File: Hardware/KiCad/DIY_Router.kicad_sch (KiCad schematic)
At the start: 21 parts, among them IC1 HLK-7628N, IC2 TPS62A06ADRLR, J1 217179-0001, SW1 SW_Push

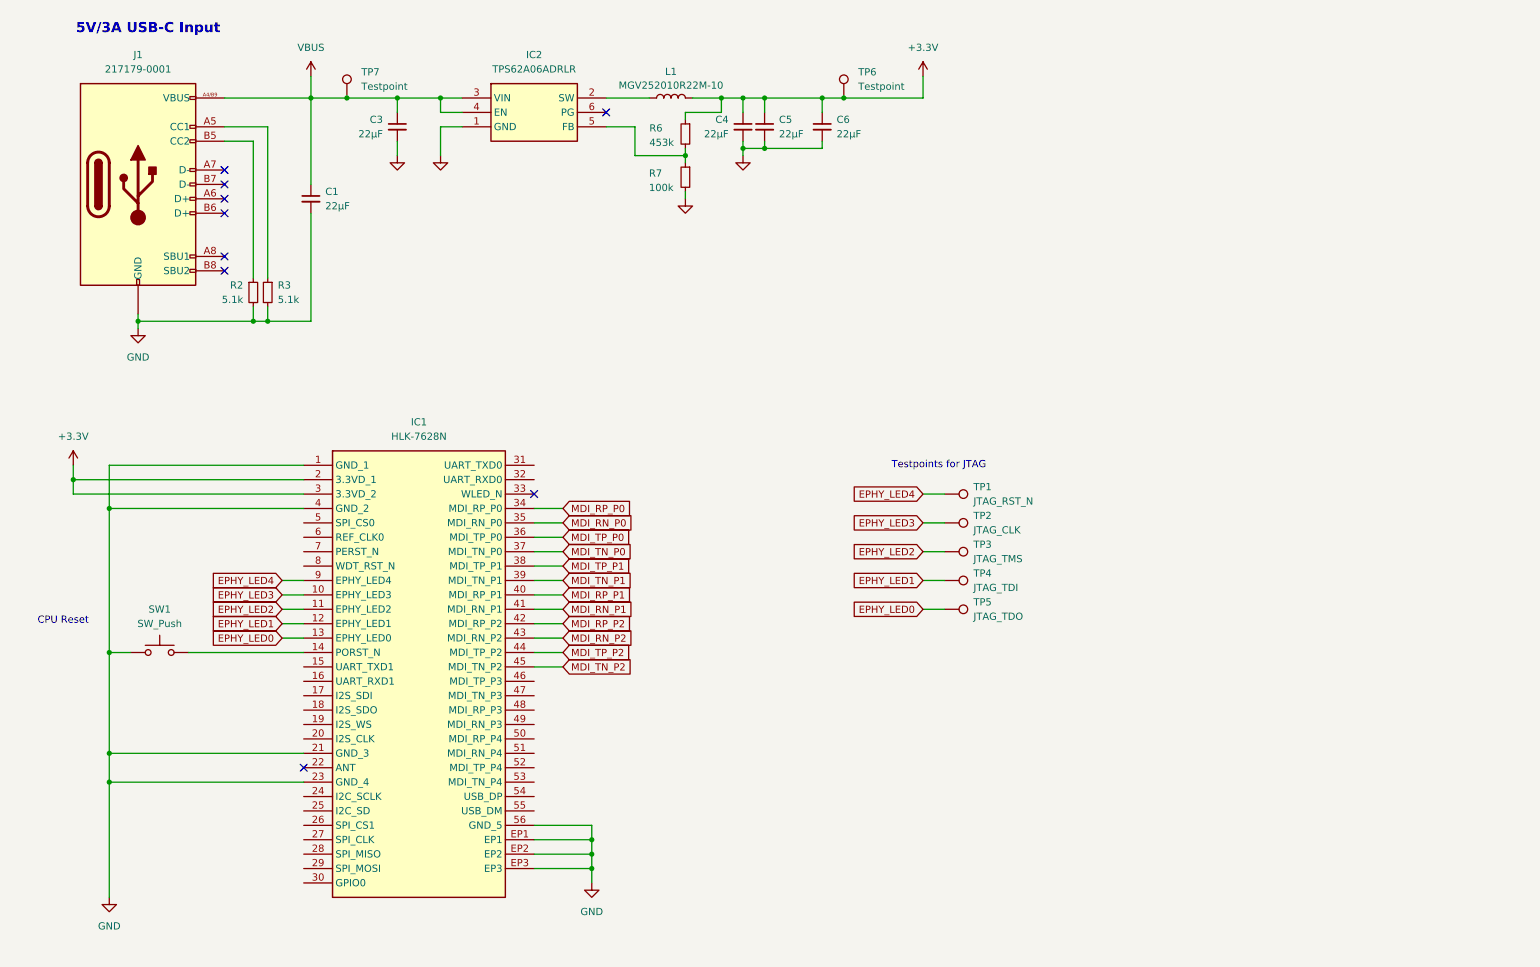
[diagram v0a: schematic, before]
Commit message: Add datasheet for MT7628 SOC Add footprints and symbol for Max Linear XR22801 USB Ethernet UART bridge Add sheet for XR22801 Add GPIO and JTAG headers in main sheet
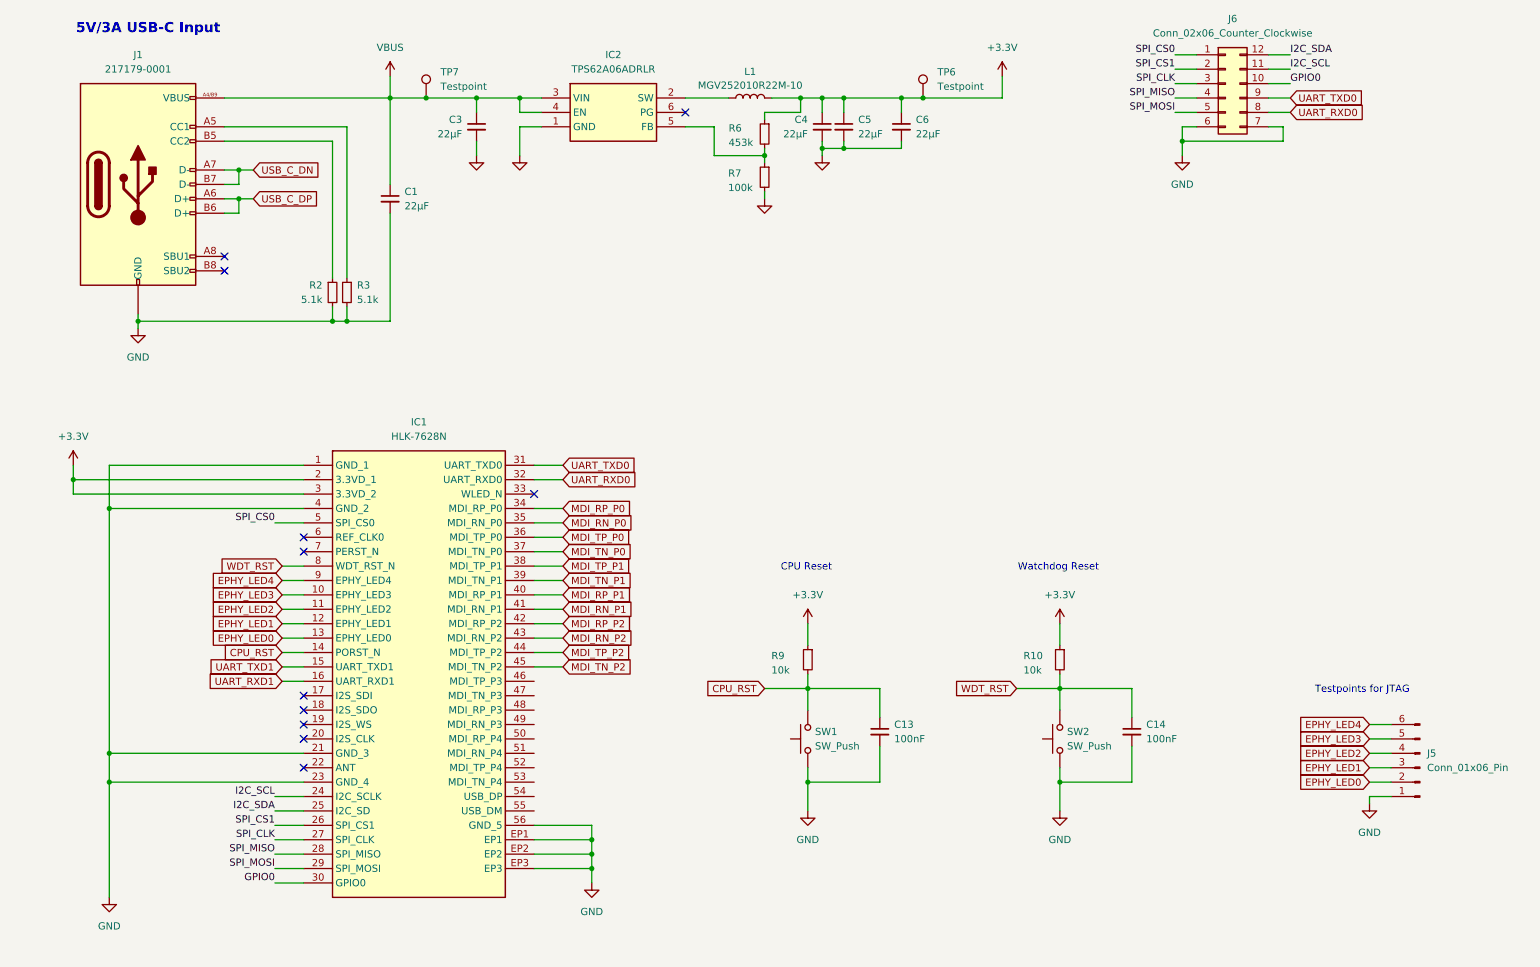
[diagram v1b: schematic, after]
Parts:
- removed TP1: JTAG_RST_N, symbol Connector:TestPoint
- removed TP2: JTAG_CLK, symbol Connector:TestPoint
- removed TP3: JTAG_TMS, symbol Connector:TestPoint
- removed TP4: JTAG_TDI, symbol Connector:TestPoint
- removed TP5: JTAG_TDO, symbol Connector:TestPoint
- added C13, C14: 100nF, Capacitor_SMD:C_0603_1608Metric, symbol Device:C_Small
- added J5: Conn_01x06_Pin, Connector_PinHeader_2.54mm:PinHeader_1x06_P2.54mm_Vertical, symbol Connector:Conn_01x06_Pin
- added J6: Conn_02x06_Counter_Clockwise, Connector_PinHeader_2.54mm:PinHeader_2x06_P2.54mm_Vertical, symbol Connector_Generic:Conn_02x06_Counter_Clockwise
- added R10, R9: 10k, Resistor_SMD:R_0402_1005Metric, symbol Device:R_Small
- added SW2: SW_Push, Button_Switch_SMD:SW_Push_1P1T-MP_NO_Horizontal_Alps_SKRTLAE010, symbol Switch:SW_Push
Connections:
- net +3.3V: now also R10.1, R9.1
- net EPHY_LED0: now also J5.2 (Pin_2)
- net EPHY_LED1: now also J5.3 (Pin_3)
- net EPHY_LED2: now also J5.4 (Pin_4)
- net EPHY_LED3: now also J5.5 (Pin_5)
- net EPHY_LED4: now also J5.6 (Pin_6)
- net GND: now also C13.2, C14.2, J5.1 (Pin_1), J6.6 (Pin_6), J6.7 (Pin_7), SW2.1
- net USB_C_DP: now reaches J1.A6 (D+)
- net USB_C_DP: now also J1.B6 (D+)
- net USB_C_DN: now reaches J1.A7 (D-)
- net USB_C_DN: now also J1.B7 (D-)
- net CPU_RST: now reaches IC1.14 (PORST_N), SW1.2
- net CPU_RST: now also C13.1, R9.2
- net UART_TXD1: now reaches IC1.15 (UART_TXD1)
- net UART_RXD1: now reaches IC1.16 (UART_RXD1)
- net I2C_SCL: now reaches IC1.24 (I2C_SCLK)
- net I2C_SCL: now also J6.11 (Pin_11)
- net I2C_SDA: now reaches IC1.25 (I2C_SD)
- net I2C_SDA: now also J6.12 (Pin_12)
- net SPI_CS1: now reaches IC1.26 (SPI_CS1)
- net SPI_CS1: now also J6.2 (Pin_2)
- net SPI_CLK: now reaches IC1.27 (SPI_CLK)
- net SPI_CLK: now also J6.3 (Pin_3)
- net SPI_MISO: now reaches IC1.28 (SPI_MISO)
- net SPI_MISO: now also J6.4 (Pin_4)
- net SPI_MOSI: now reaches IC1.29 (SPI_MOSI)
- net SPI_MOSI: now also J6.5 (Pin_5)
- net GPIO0: now reaches IC1.30 (GPIO0)
- net GPIO0: now also J6.10 (Pin_10)
- net UART_TXD0: now reaches IC1.31 (UART_TXD0)
- net UART_TXD0: now also J6.9 (Pin_9)
- net UART_RXD0: now reaches IC1.32 (UART_RXD0)
- net UART_RXD0: now also J6.8 (Pin_8)
- net SPI_CS0: now reaches IC1.5 (SPI_CS0)
- net SPI_CS0: now also J6.1 (Pin_1)
- net WDT_RST: now reaches IC1.8 (WDT_RST_N)
- net WDT_RST: now also C14.1, R10.2, SW2.2
- no-connect marks 9 -> 11
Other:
- note added: "Watchdog Reset"
- moved on the sheet: C1, C3, C4, C5, C6, IC2, L1, R2, R3, R6, R7, SW1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

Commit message: Add USB ESD protection USBLC6-2SC6Y Edit GPIO pin header
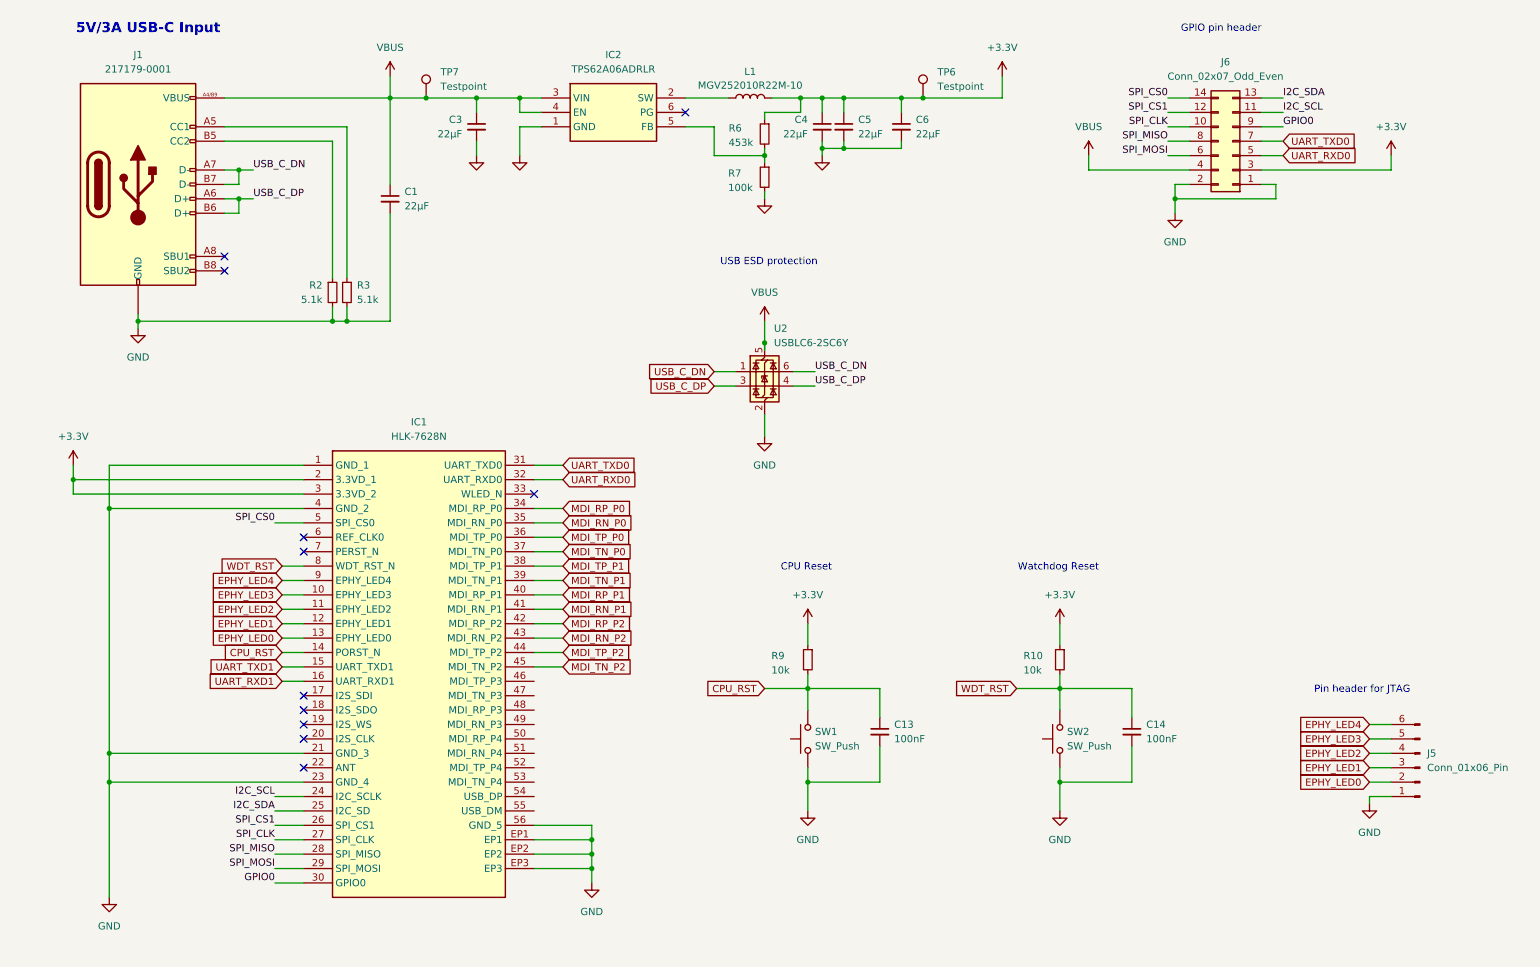
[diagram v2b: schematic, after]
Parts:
- removed J6: Conn_02x06_Counter_Clockwise, Connector_PinHeader_2.54mm:PinHeader_2x06_P2.54mm_Vertical, symbol Connector_Generic:Conn_02x06_Counter_Clockwise
- added J6: Conn_02x07_Odd_Even, Connector_PinHeader_2.54mm:PinHeader_2x07_P2.54mm_Vertical, symbol Connector_Generic:Conn_02x07_Odd_Even
- added U2: USBLC6-2SC6Y, Button_Switch_SMD:SW_DIP_SPSTx03_Slide_6.7x9.18mm_W6.73mm_P2.54mm_LowProfile_JPin, symbol Power_Protection:USBLC6-2SC6
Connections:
- net +3.3V: now also J6.3 (Pin_3)
- net GND: now also J6.1 (Pin_1), J6.2 (Pin_2), U2.2 (GND)
- net GPIO0: now also J6.9 (Pin_9)
- net I2C_SCL: now also J6.11 (Pin_11)
- net I2C_SDA: now also J6.13 (Pin_13)
- net SPI_CLK: now also J6.10 (Pin_10)
- net SPI_CS0: now also J6.14 (Pin_14)
- net SPI_CS1: now also J6.12 (Pin_12)
- net SPI_MISO: now also J6.8 (Pin_8)
- net SPI_MOSI: now also J6.6 (Pin_6)
- net UART_RXD0: now also J6.5 (Pin_5)
- net UART_TXD0: now also J6.7 (Pin_7)
- net USB_C_DN: now also U2.1 (I/O1), U2.6 (I/O1)
- net USB_C_DP: now also U2.3 (I/O2), U2.4 (I/O2)
- net VBUS: now also J6.4 (Pin_4), U2.5 (VBUS)
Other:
- note added: "GPIO pin header"
- note added: "Pin header for JTAG"
- note added: "USB ESD protection"
- note removed: "Testpoints for JTAG"

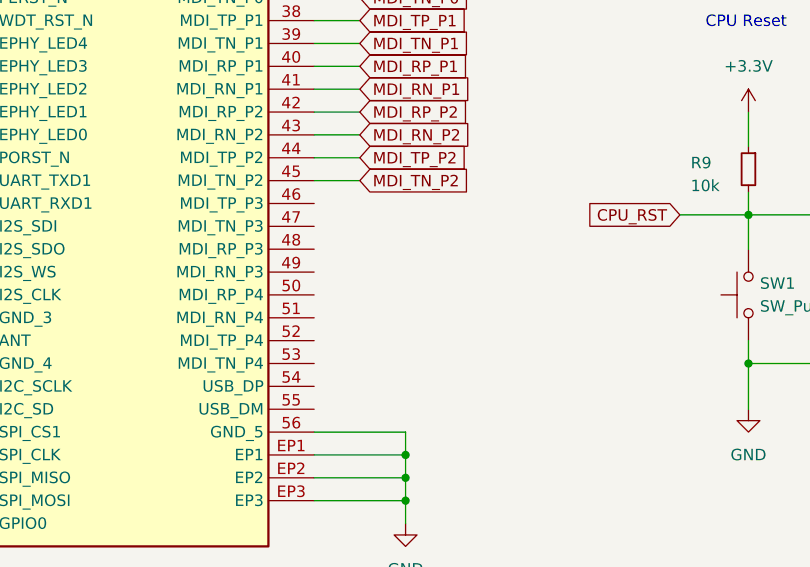
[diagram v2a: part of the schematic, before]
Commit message: USB_Bridge: add transformerless connection between usb bridge and SOM
- Ethernet: Add fourth rj45 jack
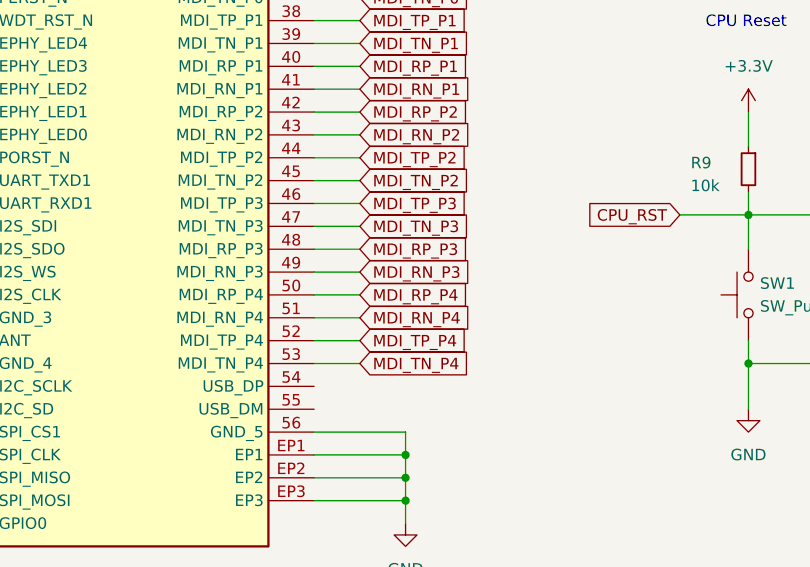
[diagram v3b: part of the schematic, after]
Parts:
- U2: footprint Button_Switch_SMD:SW_DIP_SPSTx03_Slide_6.7x9.18mm_W6.73mm_P2.54mm_LowProfile_JPin -> Package_TO_SOT_SMD:SOT-23-6
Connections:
- net MDI_TP_P3: now reaches IC1.46 (MDI_TP_P3)
- net MDI_TN_P3: now reaches IC1.47 (MDI_TN_P3)
- net MDI_RP_P3: now reaches IC1.48 (MDI_RP_P3)
- net MDI_RN_P3: now reaches IC1.49 (MDI_RN_P3)
- net MDI_RP_P4: now reaches IC1.50 (MDI_RP_P4)
- net MDI_RN_P4: now reaches IC1.51 (MDI_RN_P4)
- net MDI_TP_P4: now reaches IC1.52 (MDI_TP_P4)
- net MDI_TN_P4: now reaches IC1.53 (MDI_TN_P4)

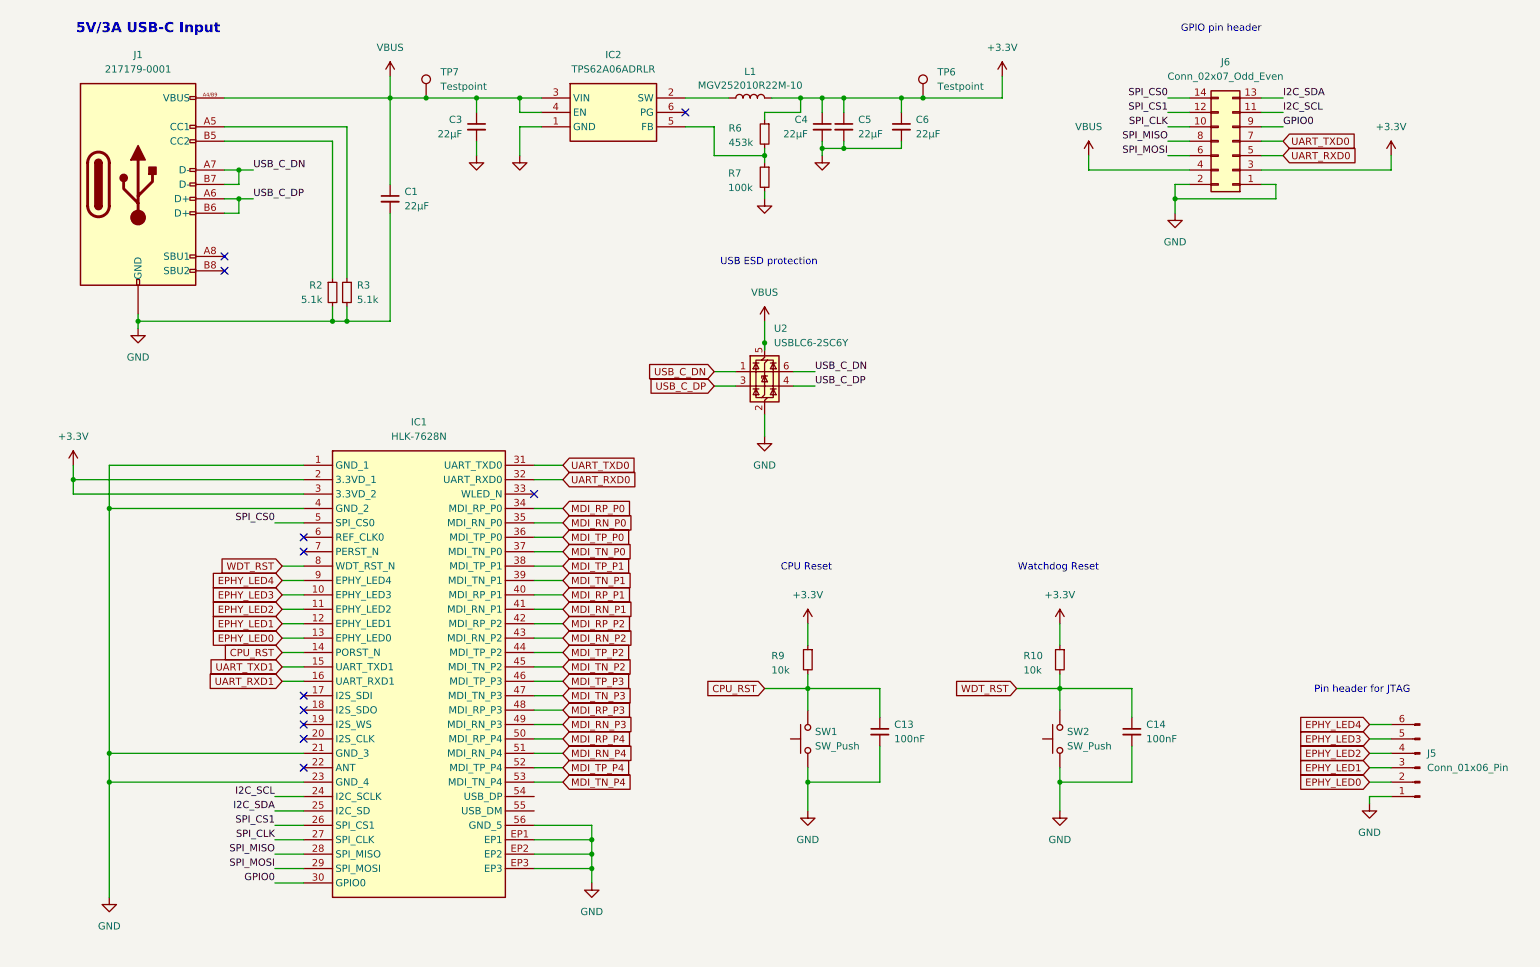
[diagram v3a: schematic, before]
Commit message: Add Mini PCIe slot TE 2041626 Add Mini PCIe mounting holes and board mounting holes Add nano SIM card slot SIM8066 Add SIM ESD and EMI filter EMIF03-SIM02M8 Add USB Hub USB2422 Add USB A port with ESD chip Add README.md for details about HLK-7628N Edit text above ethernet ports
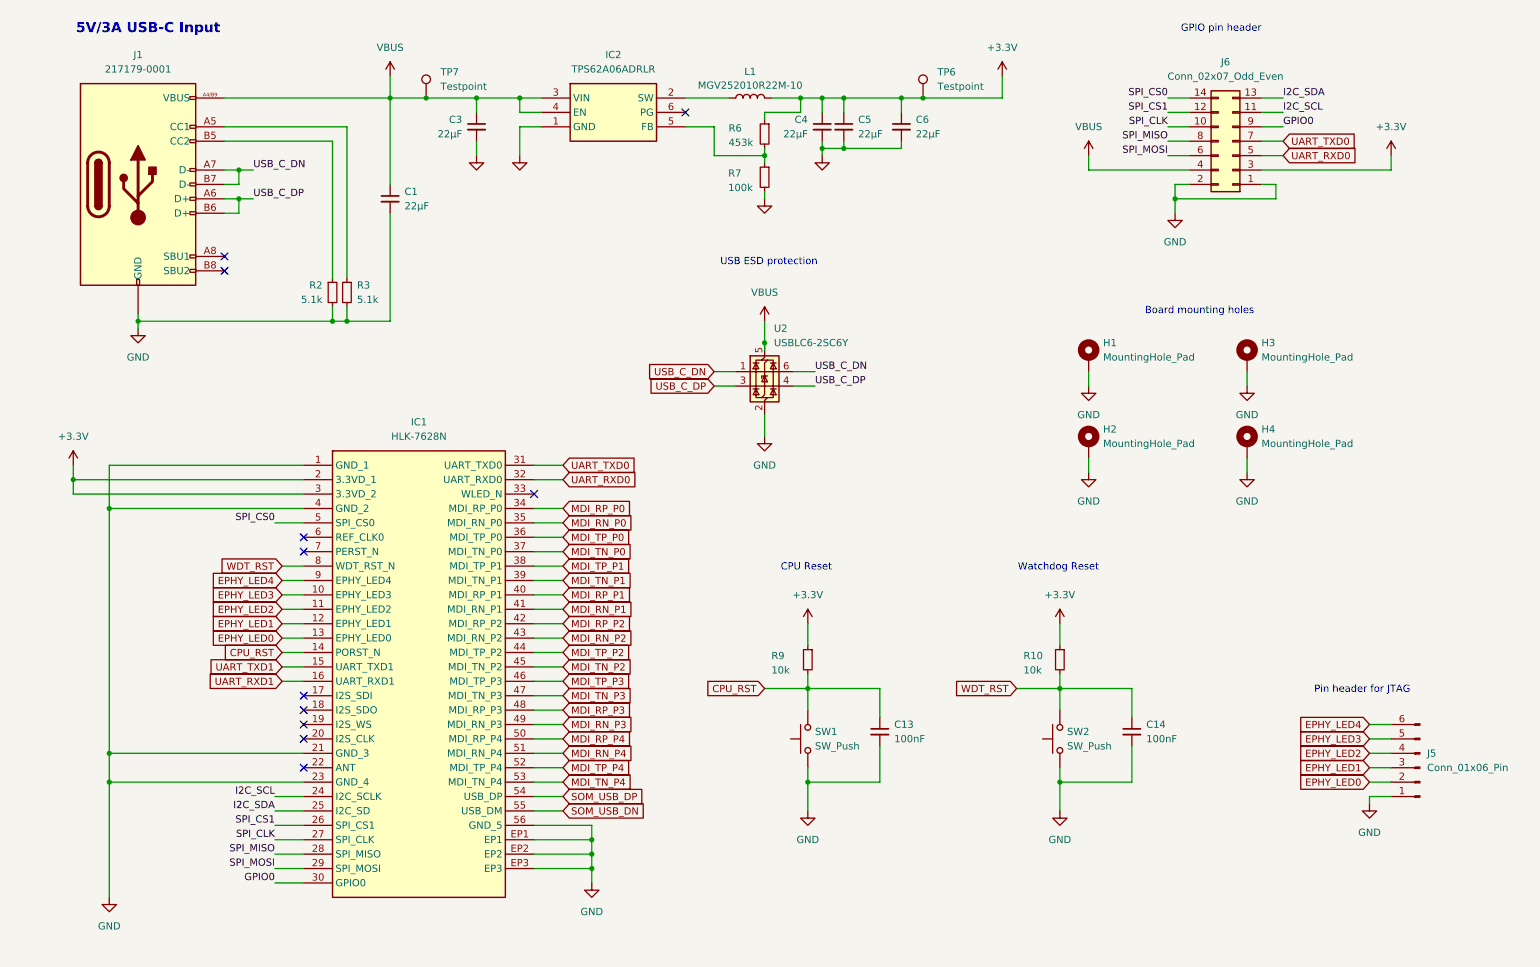
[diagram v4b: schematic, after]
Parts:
- added H1, H2, H3, H4: MountingHole_Pad, MountingHole:MountingHole_3.2mm_M3_DIN965_Pad_TopBottom, symbol Mechanical:MountingHole_Pad
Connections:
- net GND: now also H1.1, H2.1, H3.1, H4.1
- net SOM_USB_DP: now reaches IC1.54 (USB_DP)
- net SOM_USB_DN: now reaches IC1.55 (USB_DM)
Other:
- note added: "Board mounting holes"
